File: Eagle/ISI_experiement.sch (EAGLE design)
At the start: 14 parts, among them IC1 4009N, IC2 4174D, IC3 4030D

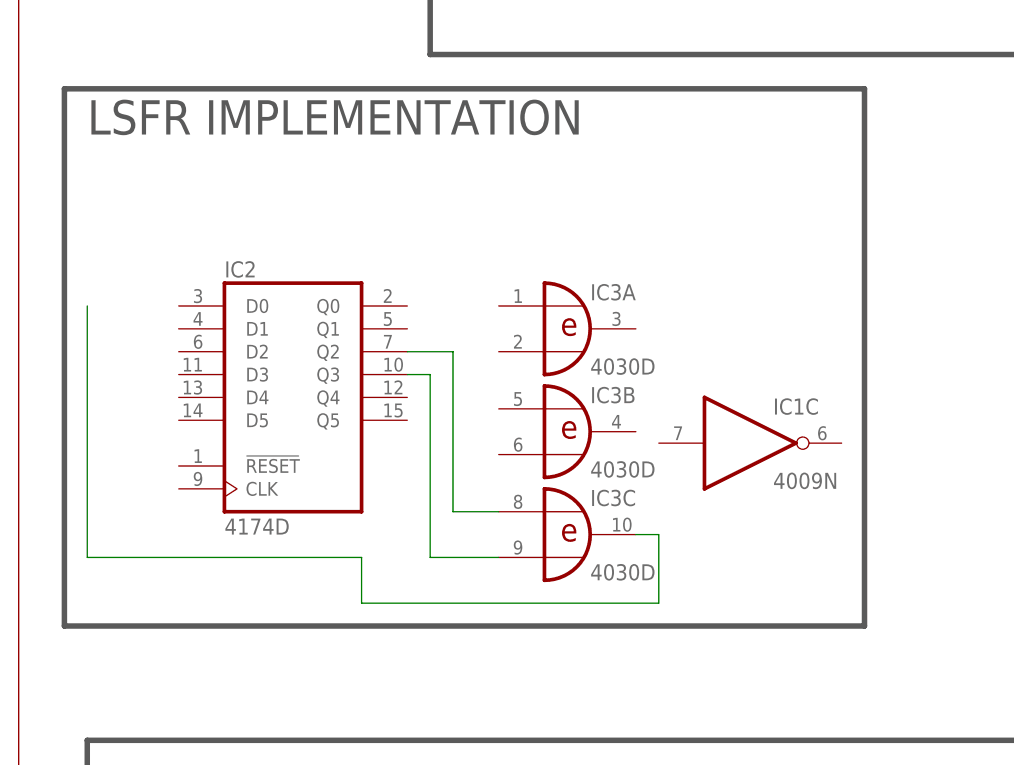
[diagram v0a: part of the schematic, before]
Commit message: changed flip-flop
changed flip flop to ordered part, original part was not available at
DigiKey
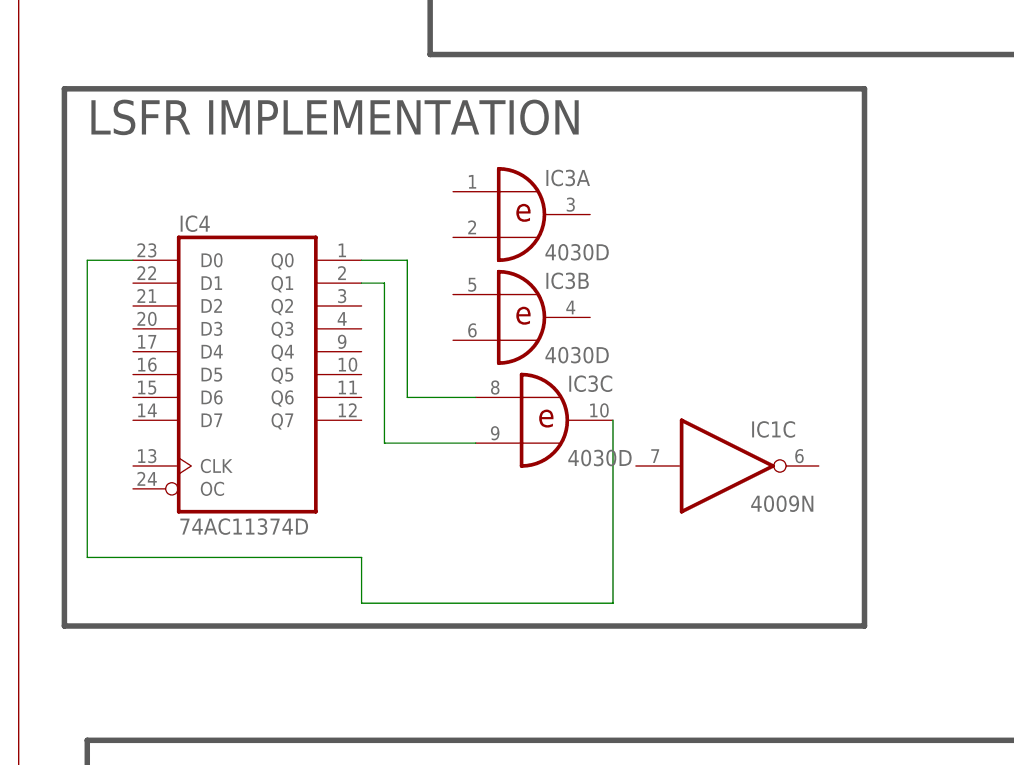
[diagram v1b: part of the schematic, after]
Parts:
- removed IC2: 4174D, 40xx:4174D
- added IC4: 74AC11374D, 74ac-logic:74AC11374D
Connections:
- net N$12: now also IC4A.D0
- net N$8: now also IC4A.Q1; no longer IC2G$1.Q3
- net N$9: now also IC4A.Q0; no longer IC2G$1.Q2
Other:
- moved on the sheet: IC1C, IC3A, IC3B, IC3C
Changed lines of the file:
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@@
 <grid distance="0.1" unitdist="inch" unit="inch" style="lines" multiple="1" display="no" altdistance="0.01" altunitdist="inch" altunit="inch"/>
 <layers>
-<layer number="1" name="Top" color="4" fill="1" visible="yes" active="no"/>
-<layer number="16" name="Bottom" color="1" fill="1" visible="yes" active="no"/>
-<layer number="17" name="Pads" color="2" fill="1" visible="yes" active="no"/>
-<layer number="18" name="Vias" color="2" fill="1" visible="yes" active="no"/>
-<layer number="19" name="Unrouted" color="6" fill="1" visible="yes" active="no"/>
-<layer number="20" name="Dimension" color="15" fill="1" visible="yes" active="no"/>
-<layer number="21" name="tPlace" color="7" fill="1" visible="yes" active="no"/>
-<layer number="22" name="bPlace" color="7" fill="1" visible="yes" active="no"/>
-<layer number="23" name="tOrigins" color="15" fill="1" visible="yes" active="no"/>
-<layer number="24" name="bOrigins" color="15" fill="1" visible="yes" active="no"/>
-<layer number="25" name="tNames" color="7" fill="1" visible="yes" active="no"/>
-<layer number="26" name="bNames" color="7" fill="1" visible="yes" active="no"/>
-<layer number="27" name="tValues" color="7" fill="1" visible="yes" active="no"/>
-<layer number="28" name="bValues" color="7" fill="1" visible="yes" active="no"/>
+<layer number="1" name="Top" color="4" fill="1" visible="no" active="no"/>
+<layer number="16" name="Bottom" color="1" fill="1" visible="no" active="no"/>
+<layer number="17" name="Pads" color="2" fill="1" visible="no" active="no"/>
+<layer number="18" name="Vias" color="2" fill="1" visible="no" active="no"/>
+<layer number="19" name="Unrouted" color="6" fill="1" visible="no" active="no"/>
+<layer number="20" name="Dimension" color="15" fill="1" visible="no" active="no"/>
+<layer number="21" name="tPlace" color="7" fill="1" visible="no" active="no"/>
+<layer number="22" name="bPlace" color="7" fill="1" visible="no" active="no"/>
+<layer number="23" name="tOrigins" color="15" fill="1" visible="no" active="no"/>
+<layer number="24" name="bOrigins" color="15" fill="1" visible="no" active="no"/>
+<layer number="25" name="tNames" color="7" fill="1" visible="no" active="no"/>
+<layer number="26" name="bNames" color="7" fill="1" visible="no" active="no"/>
+<layer number="27" name="tValues" color="7" fill="1" visible="no" active="no"/>
+<layer number="28" name="bValues" color="7" fill="1" visible="no" active="no"/>
 <layer number="29" name="tStop" color="7" fill="3" visible="no" active="no"/>
 <layer number="30" name="bStop" color="7" fill="6" visible="no" active="no"/>
@@
 <layer number="35" name="tGlue" color="7" fill="4" visible="no" active="no"/>
 <layer number="36" name="bGlue" color="7" fill="5" visible="no" active="no"/>
-<layer number="37" name="tTest" color="7" fill="1" visible="yes" active="no"/>
-<layer number="38" name="bTest" color="7" fill="1" visible="yes" active="no"/>
+<layer number="37" name="tTest" color="7" fill="1" visible="no" active="no"/>
+<layer number="38" name="bTest" color="7" fill="1" visible="no" active="no"/>
 <layer number="39" name="tKeepout" color="4" fill="11" visible="no" active="no"/>
 <layer number="40" name="bKeepout" color="1" fill="11" visible="no" active="no"/>
@@
 <layer number="44" name="Drills" color="7" fill="1" visible="no" active="no"/>
 <layer number="45" name="Holes" color="7" fill="1" visible="no" active="no"/>
-<layer number="46" name="Milling" color="3" fill="1" visible="yes" active="no"/>
-<layer number="47" name="Measures" color="7" fill="1" visible="yes" active="no"/>
-<layer number="48" name="Document" color="7" fill="1" visible="yes" active="no"/>
-<layer number="49" name="Reference" color="7" fill="1" visible="yes" active="no"/>
-<layer number="51" name="tDocu" color="7" fill="1" visible="yes" active="no"/>
-<layer number="52" name="bDocu" color="7" fill="1" visible="yes" active="no"/>
+<layer number="46" name="Milling" color="3" fill="1" visible="no" active="no"/>
+<layer number="47" name="Measures" color="7" fill="1" visible="no" active="no"/>
+<layer number="48" name="Document" color="7" fill="1" visible="no" active="no"/>
+<layer number="49" name="Reference" color="7" fill="1" visible="no" active="no"/>
+<layer number="51" name="tDocu" color="7" fill="1" visible="no" active="no"/>
+<layer number="52" name="bDocu" color="7" fill="1" visible="no" active="no"/>
 <layer number="90" name="Modules" color="5" fill="1" visible="yes" active="yes"/>
 <layer number="91" name="Nets" color="2" fill="1" visible="yes" active="yes"/>
@@
 <part name="GND1" library="supply1" deviceset="GND" device=""/>
 <part name="P+1" library="supply1" deviceset="VCC" device=""/>
-<part name="IC2" library="40xx" deviceset="4174" device="D"/>
 <part name="IC3" library="40xx" deviceset="4030" device="D"/>
+<part name="IC4" library="74ac-logic" deviceset="74AC11374" device="D"/>
 </parts>
 <sheets>
@@
 <instance part="P+1" gate="VCC" x="25.781" y="43.942"/>
 <instance part="IC1" gate="P" x="22.86" y="30.48"/>
-<instance part="IC2" gate="G$1" x="30.48" y="99.06"/>
-<instance part="IC3" gate="A" x="60.96" y="106.68"/>
-<instance part="IC3" gate="B" x="60.96" y="95.25"/>
-<instance part="IC3" gate="C" x="60.96" y="83.82"/>
-<instance part="IC1" gate="C" x="81.28" y="93.98"/>
+<instance part="IC3" gate="A" x="55.88" y="119.38"/>
+<instance part="IC3" gate="B" x="55.88" y="107.95"/>
+<instance part="IC3" gate="C" x="58.42" y="96.52"/>
+<instance part="IC1" gate="C" x="78.74" y="91.44"/>
+<instance part="IC4" gate="A" x="25.4" y="101.6"/>
 </instances>
 <busses>
@@
 <segment>
 <pinref part="IC3" gate="C" pin="I1"/>
-<wire x1="45.72" y1="81.28" x2="53.34" y2="81.28" width="0.1524" layer="91"/>
-<pinref part="IC2" gate="G$1" pin="Q3"/>
-<wire x1="43.18" y1="101.6" x2="45.72" y2="101.6" width="0.1524" layer="91"/>
-<wire x1="45.72" y1="101.6" x2="45.72" y2="81.28" width="0.1524" layer="91"/>
+<wire x1="40.64" y1="93.98" x2="50.8" y2="93.98" width="0.1524" layer="91"/>
+<wire x1="40.64" y1="111.76" x2="40.64" y2="93.98" width="0.1524" layer="91"/>
+<pinref part="IC4" gate="A" pin="Q1"/>
+<wire x1="38.1" y1="111.76" x2="40.64" y2="111.76" width="0.1524" layer="91"/>
 </segment>
 </net>
@@
 <segment>
 <pinref part="IC3" gate="C" pin="I0"/>
-<wire x1="53.34" y1="86.36" x2="48.26" y2="86.36" width="0.1524" layer="91"/>
-<wire x1="48.26" y1="86.36" x2="48.26" y2="104.14" width="0.1524" layer="91"/>
-<pinref part="IC2" gate="G$1" pin="Q2"/>
-<wire x1="48.26" y1="104.14" x2="43.18" y2="104.14" width="0.1524" layer="91"/>
+<wire x1="50.8" y1="99.06" x2="43.18" y2="99.06" width="0.1524" layer="91"/>
+<wire x1="43.18" y1="99.06" x2="43.18" y2="114.3" width="0.1524" layer="91"/>
+<pinref part="IC4" gate="A" pin="Q0"/>
+<wire x1="43.18" y1="114.3" x2="38.1" y2="114.3" width="0.1524" layer="91"/>
 </segment>
 </net>
@@
 <segment>
 <pinref part="IC3" gate="C" pin="O"/>
-<wire x1="68.58" y1="83.82" x2="71.12" y2="83.82" width="0.1524" layer="91"/>
-<wire x1="71.12" y1="83.82" x2="71.12" y2="76.2" width="0.1524" layer="91"/>
-<wire x1="71.12" y1="76.2" x2="38.1" y2="76.2" width="0.1524" layer="91"/>
+<wire x1="66.04" y1="96.52" x2="66.04" y2="76.2" width="0.1524" layer="91"/>
+<wire x1="66.04" y1="76.2" x2="38.1" y2="76.2" width="0.1524" layer="91"/>
 <wire x1="38.1" y1="76.2" x2="38.1" y2="81.28" width="0.1524" layer="91"/>
 <wire x1="38.1" y1="81.28" x2="7.62" y2="81.28" width="0.1524" layer="91"/>
-<wire x1="7.62" y1="81.28" x2="7.62" y2="109.22" width="0.1524" layer="91"/>
-</segment>
-</net>
+<wire x1="7.62" y1="81.28" x2="7.62" y2="114.3" width="0.1524" layer="91"/>
+<pinref part="IC4" gate="A" pin="D0"/>
+<wire x1="12.7" y1="114.3" x2="7.62" y2="114.3" width="0.1524" layer="91"/>
+</segment>
+</net>

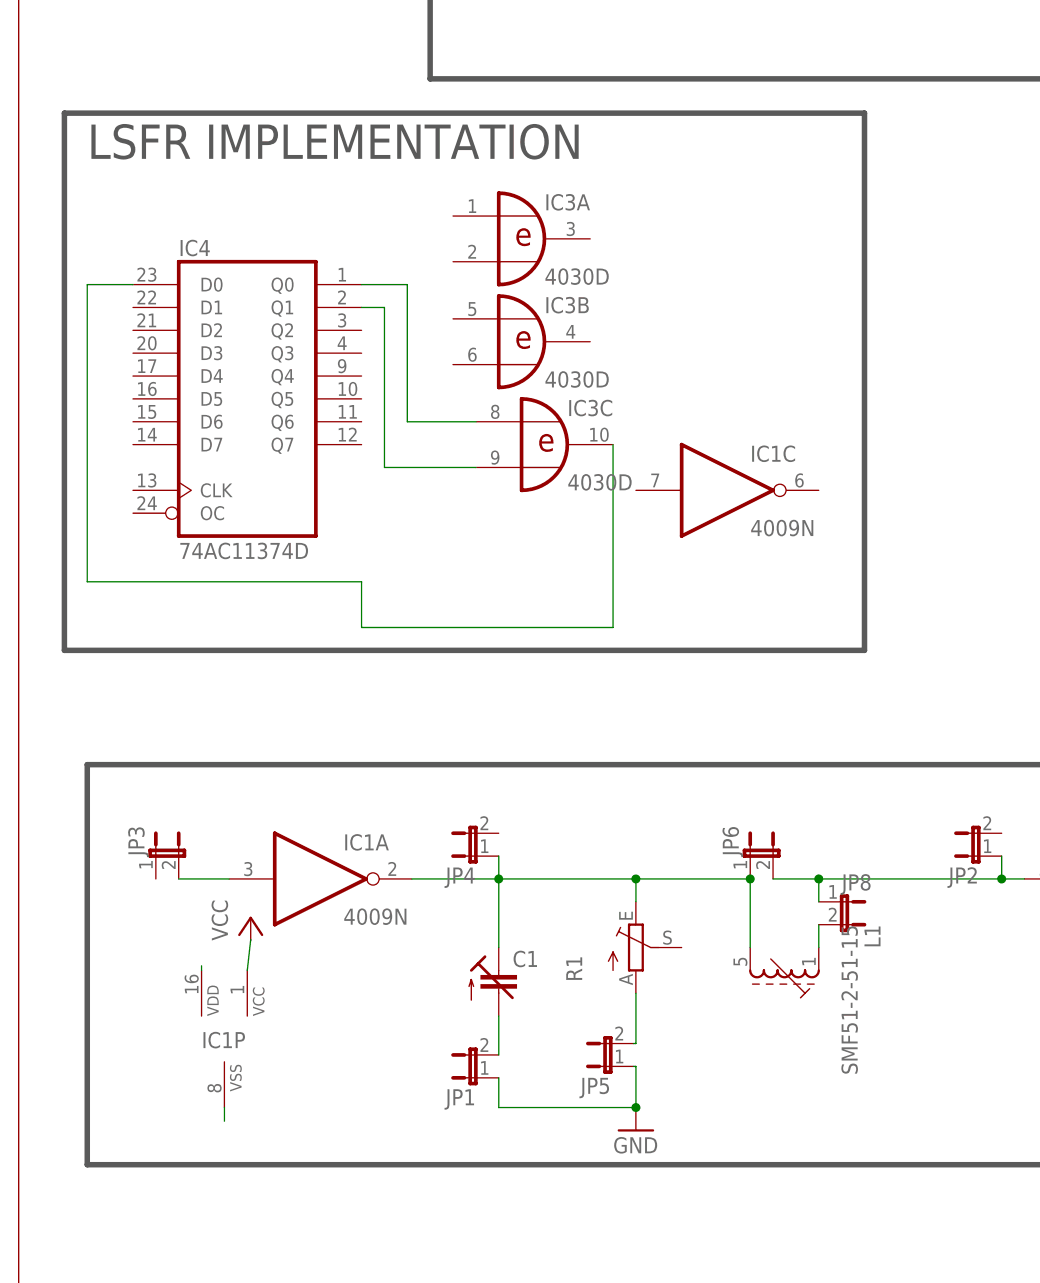
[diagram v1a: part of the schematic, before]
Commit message: ISI part library
Started part library with schematic and parts both on mm to match what
Kris wanted
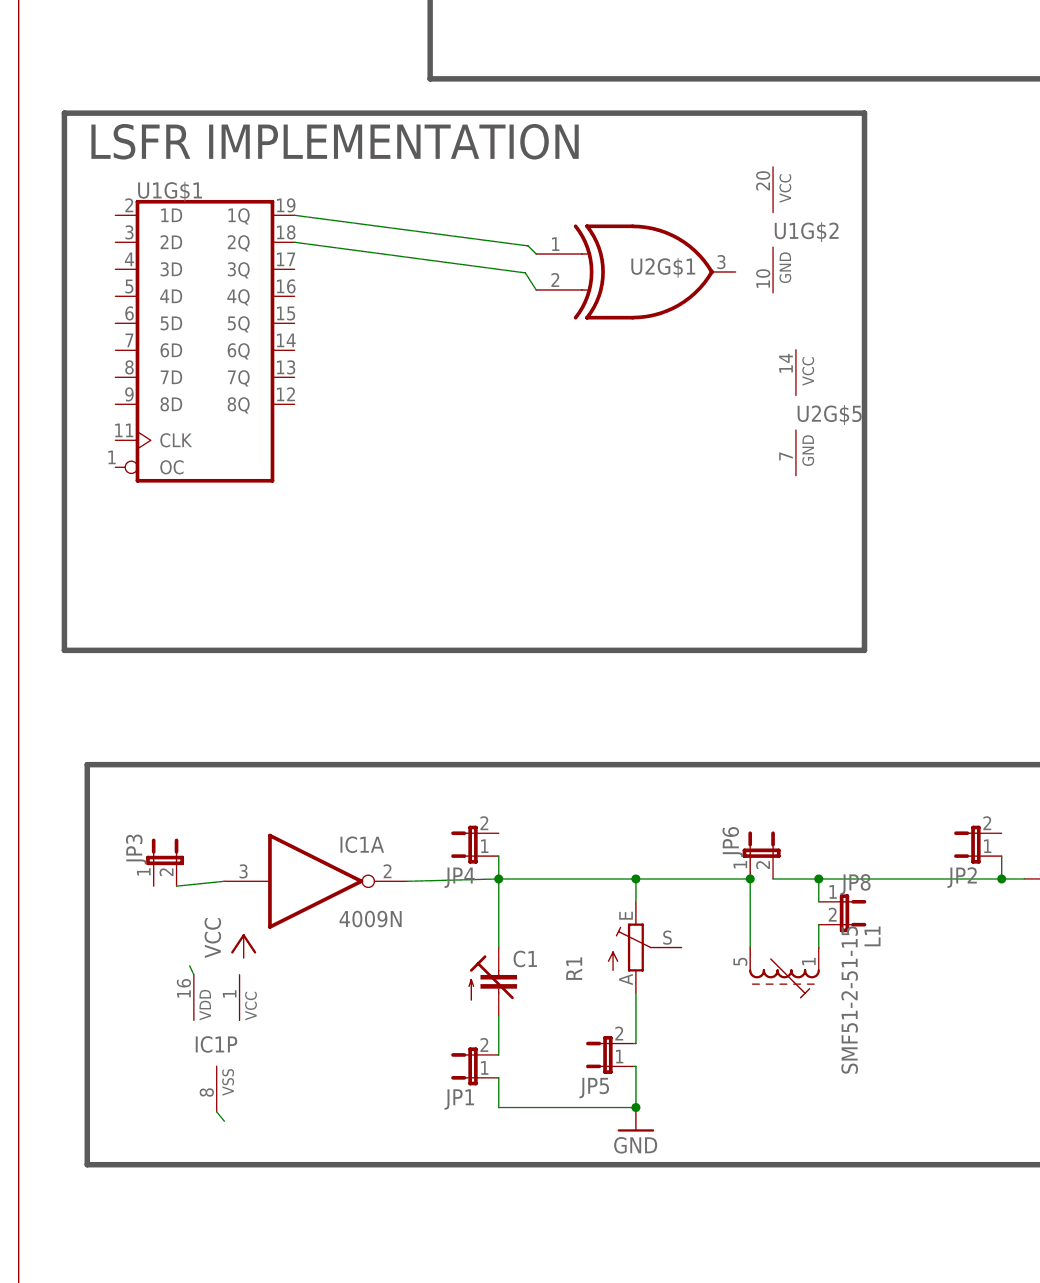
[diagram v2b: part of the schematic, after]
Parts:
- removed IC3: 4030D, 40xx:4030D
- removed IC4: 74AC11374D, 74ac-logic:74AC11374D
- added U1: (no value), E3VB_ISI:74AC574
- added U2: 7486, E3VB_ISI:7486
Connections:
- removed net N$11: IC1P.VCC
- removed net N$12: IC3C.O, IC4A.D0
- net N$8: now also U1G$1.1Q, U2G$1.I0; no longer IC3C.I1, IC4A.Q1
- net N$9: now also U1G$1.2Q, U2G$1.I1; no longer IC3C.I0, IC4A.Q0
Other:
- moved on the sheet: IC1A, IC1P, JP3
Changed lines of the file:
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@@
 <setting verticaltext="up"/>
 </settings>
-<grid distance="0.1" unitdist="inch" unit="inch" style="lines" multiple="1" display="no" altdistance="0.01" altunitdist="inch" altunit="inch"/>
+<grid distance="0.1" unitdist="mm" unit="mm" style="lines" multiple="1" display="yes" altdistance="0.1" altunitdist="mm" altunit="mm"/>
 <layers>
 <layer number="1" name="Top" color="4" fill="1" visible="no" active="no"/>
@@
 <part name="GND1" library="supply1" deviceset="GND" device=""/>
 <part name="P+1" library="supply1" deviceset="VCC" device=""/>
-<part name="IC3" library="40xx" deviceset="4030" device="D"/>
-<part name="IC4" library="74ac-logic" deviceset="74AC11374" device="D"/>
+<part name="U1" library="E3VB_ISI" deviceset="74*574" device="" technology="AC"/>
+<part name="U2" library="E3VB_ISI" deviceset="74*86*" device=""/>
 </parts>
 <sheets>
@@
 <instance part="JP1" gate="A" x="50.8" y="26.162" rot="R90"/>
 <instance part="JP2" gate="A" x="106.68" y="50.8" rot="R90"/>
-<instance part="JP3" gate="A" x="15.24" y="50.8"/>
+<instance part="JP3" gate="A" x="15" y="50"/>
 <instance part="JP4" gate="A" x="50.8" y="50.8" rot="R90"/>
 <instance part="JP5" gate="A" x="65.786" y="27.432" rot="R90"/>
-<instance part="IC1" gate="A" x="33.528" y="48.26"/>
+<instance part="IC1" gate="A" x="33" y="48"/>
 <instance part="JP6" gate="A" x="81.28" y="50.8"/>
 <instance part="R1" gate="1" x="68.58" y="40.64"/>
@@
 <instance part="JP8" gate="A" x="91.44" y="45.72" rot="R270"/>
 <instance part="GND1" gate="1" x="68.58" y="20.32"/>
-<instance part="P+1" gate="VCC" x="25.781" y="43.942"/>
-<instance part="IC1" gate="P" x="22.86" y="30.48"/>
-<instance part="IC3" gate="A" x="55.88" y="119.38"/>
-<instance part="IC3" gate="B" x="55.88" y="107.95"/>
-<instance part="IC3" gate="C" x="58.42" y="96.52"/>
-<instance part="IC1" gate="C" x="78.74" y="91.44"/>
-<instance part="IC4" gate="A" x="25.4" y="101.6"/>
+<instance part="P+1" gate="VCC" x="25" y="42"/>
+<instance part="IC1" gate="P" x="22" y="30"/>
+<instance part="U1" gate="G$2" x="83.82" y="119.38"/>
+<instance part="U2" gate="G$1" x="69.5" y="115.7"/>
+<instance part="U2" gate="G$5" x="86.36" y="99.06"/>
+<instance part="U1" gate="G$1" x="20.7" y="108"/>
 </instances>
 <busses>
 </busses>
 <nets>
-<net name="N$11" class="0">
-<segment>
-<wire x1="25.781" y1="41.529" x2="25.4" y2="38.1" width="0.1524" layer="91"/>
-<pinref part="IC1" gate="P" pin="VCC"/>
-</segment>
-</net>
 <net name="GND" class="0">
 <segment>
@@
 <segment>
 <pinref part="IC1" gate="P" pin="VSS"/>
-<wire x1="22.86" y1="22.86" x2="22.86" y2="21.336" width="0.1524" layer="91"/>
+<wire x1="22" y1="22.38" x2="22.86" y2="21.336" width="0.1524" layer="91"/>
 </segment>
 </net>
@@
 <pinref part="JP3" gate="A" pin="2"/>
 <pinref part="IC1" gate="A" pin="I"/>
-<wire x1="17.78" y1="48.26" x2="23.368" y2="48.26" width="0.1524" layer="91"/>
+<wire x1="17.54" y1="47.46" x2="22.84" y2="48" width="0.1524" layer="91"/>
 </segment>
 </net>
@@
 <segment>
 <pinref part="IC1" gate="A" pin="O"/>
-<wire x1="43.688" y1="48.26" x2="53.34" y2="48.26" width="0.1524" layer="91"/>
+<wire x1="43.16" y1="48" x2="53.34" y2="48.26" width="0.1524" layer="91"/>
 <pinref part="JP6" gate="A" pin="1"/>
 <wire x1="53.34" y1="48.26" x2="68.58" y2="48.26" width="0.1524" layer="91"/>
@@
 <segment>
 <pinref part="IC1" gate="P" pin="VDD"/>
-<wire x1="20.32" y1="38.1" x2="20.32" y2="38.608" width="0.1524" layer="91"/>
+<wire x1="19.46" y1="37.62" x2="19" y2="38.608" width="0.1524" layer="91"/>
 </segment>
 </net>
 <net name="N$8" class="0">
 <segment>
-<pinref part="IC3" gate="C" pin="I1"/>
-<wire x1="40.64" y1="93.98" x2="50.8" y2="93.98" width="0.1524" layer="91"/>
-<wire x1="40.64" y1="111.76" x2="40.64" y2="93.98" width="0.1524" layer="91"/>
-<pinref part="IC4" gate="A" pin="Q1"/>
-<wire x1="38.1" y1="111.76" x2="40.64" y2="111.76" width="0.1524" layer="91"/>
+<pinref part="U2" gate="G$1" pin="I0"/>
+<wire x1="30.66" y1="122" x2="56.6" y2="118.6" width="0.1524" layer="91"/>
+<wire x1="56.6" y1="118.6" x2="57.5" y2="117.7" width="0.1524" layer="91"/>
+<pinref part="U1" gate="G$1" pin="1Q"/>
 </segment>
 </net>
 <net name="N$9" class="0">
 <segment>
-<pinref part="IC3" gate="C" pin="I0"/>
-<wire x1="50.8" y1="99.06" x2="43.18" y2="99.06" width="0.1524" layer="91"/>
-<wire x1="43.18" y1="99.06" x2="43.18" y2="114.3" width="0.1524" layer="91"/>
-<pinref part="IC4" gate="A" pin="Q0"/>
-<wire x1="43.18" y1="114.3" x2="38.1" y2="114.3" width="0.1524" layer="91"/>
-</segment>
-</net>
-<net name="N$12" class="0">
-<segment>
-<pinref part="IC3" gate="C" pin="O"/>
-<wire x1="66.04" y1="96.52" x2="66.04" y2="76.2" width="0.1524" layer="91"/>
-<wire x1="66.04" y1="76.2" x2="38.1" y2="76.2" width="0.1524" layer="91"/>
-<wire x1="38.1" y1="76.2" x2="38.1" y2="81.28" width="0.1524" layer="91"/>
-<wire x1="38.1" y1="81.28" x2="7.62" y2="81.28" width="0.1524" layer="91"/>
-<wire x1="7.62" y1="81.28" x2="7.62" y2="114.3" width="0.1524" layer="91"/>
-<pinref part="IC4" gate="A" pin="D0"/>
-<wire x1="12.7" y1="114.3" x2="7.62" y2="114.3" width="0.1524" layer="91"/>
-</segment>
-</net>
+<wire x1="57.5" y1="113.7" x2="56.3" y2="115.6" width="0.1524" layer="91"/>
+<wire x1="56.3" y1="115.6" x2="30.66" y2="119" width="0.1524" layer="91"/>
+<pinref part="U2" gate="G$1" pin="I1"/>
+<pinref part="U1" gate="G$1" pin="2Q"/>
+</segment>
+</net>
